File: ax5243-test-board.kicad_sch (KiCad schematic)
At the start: 39 parts, among them J1 Conn_Coaxial, J2 Conn_01x15, J3 Conn_01x15, U1 AX5243, X1 12MHz

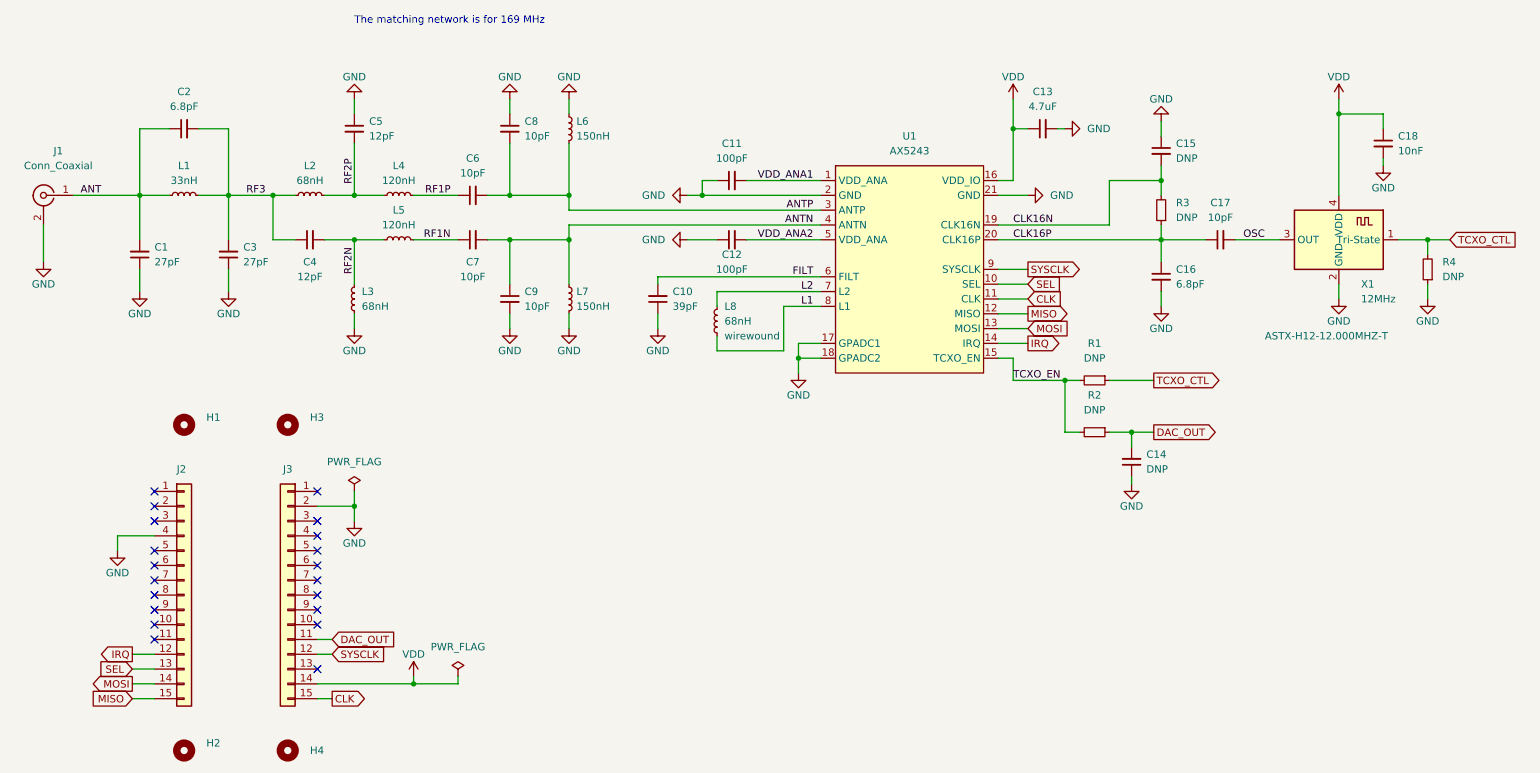
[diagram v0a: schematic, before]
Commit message: Add part numbers and Digikey SKUs
Also change TCXO frequency to 26 MHz.
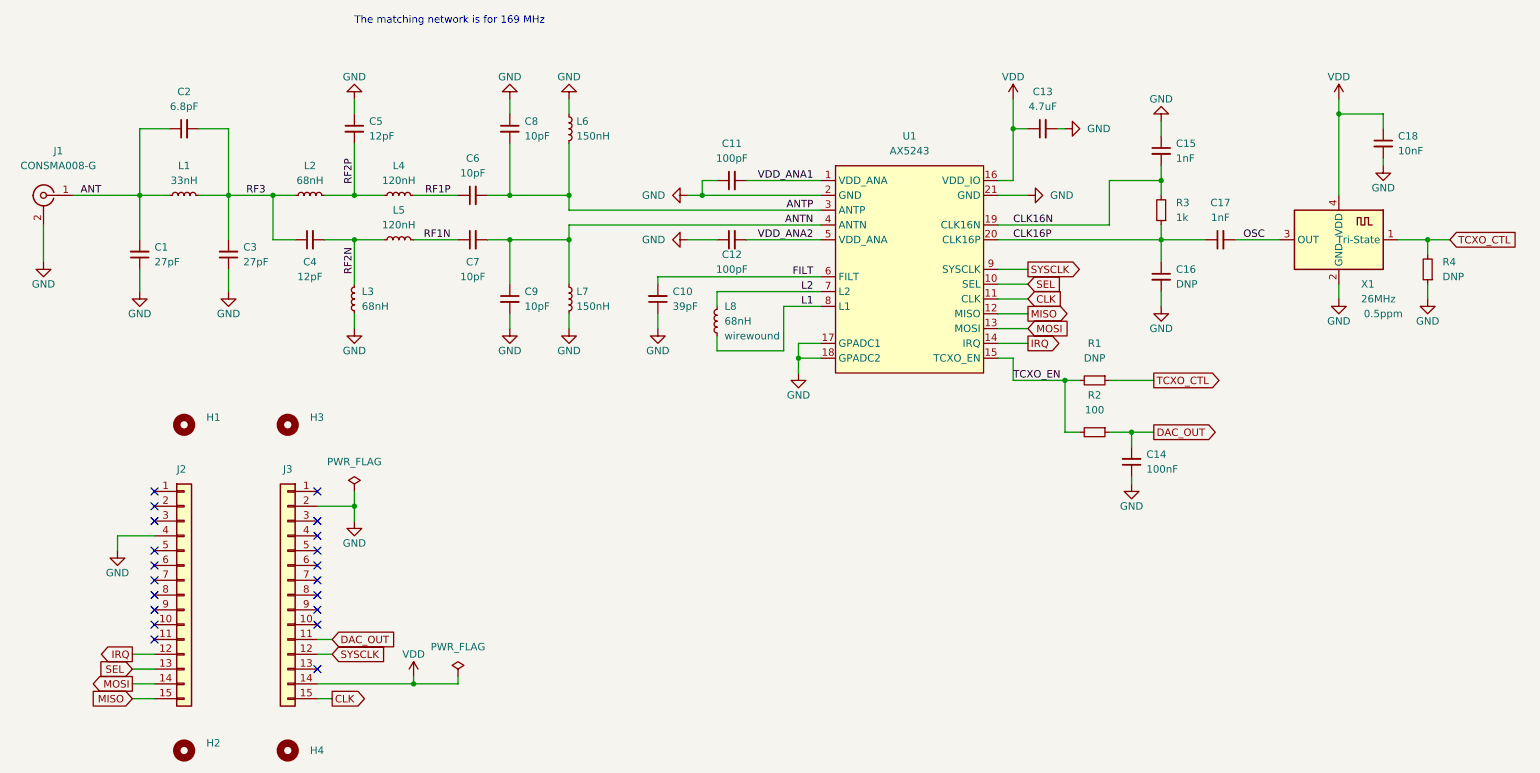
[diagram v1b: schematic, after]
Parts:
- C1, C3: MFT Name (none) -> Murata; MFT Number (none) -> GJM1555C1H270FB01D; SKU (none) -> 490-16380-1-ND; Vendor (none) -> Digikey
- C10: MFT Name (none) -> Murata; MFT Number (none) -> GJM1555C1H390JB01D; SKU (none) -> 490-17673-1-ND; Vendor (none) -> Digikey
- C11, C12: MFT Name (none) -> Murata; MFT Number (none) -> GCM1555C1H101GA16D; SKU (none) -> 490-GCM1555C1H101GA16DCT-ND; Vendor (none) -> Digikey
- C13: MFT Name (none) -> Murata; MFT Number (none) -> GRM188R61E475KE11D; SKU (none) -> 490-7203-1-ND; Vendor (none) -> Digikey
- C14: value DNP -> 100nF; MFT Name (none) -> Murata; MFT Number (none) -> GRM155R71H104KE14D; SKU (none) -> 490-10700-1-ND; Vendor (none) -> Digikey
- C15: value DNP -> 1nF; MFT Name (none) -> Murata; MFT Number (none) -> GRM1555C1H102GA01D; SKU (none) -> 490-8181-1-ND; Vendor (none) -> Digikey
- C16: value 6.8pF -> DNP; Config (none) -> DNP
- C17: value 10pF -> 1nF; MFT Name (none) -> Murata; MFT Number (none) -> GRM1555C1H102GA01D; SKU (none) -> 490-8181-1-ND; Vendor (none) -> Digikey
- C18: MFT Name (none) -> Murata; MFT Number (none) -> GRM155R71H103KA88J; SKU (none) -> 490-6351-1-ND; Vendor (none) -> Digikey
- C2: MFT Name (none) -> Murata; MFT Number (none) -> GJM1555C1H6R8CB01D; SKU (none) -> 490-3106-1-ND; Vendor (none) -> Digikey
- C4, C5: MFT Name (none) -> Murata; MFT Number (none) -> GJM1555C1H120JB01D; SKU (none) -> 490-3115-1-ND; Vendor (none) -> Digikey
- C6, C7, C8, C9: MFT Name (none) -> Murata; MFT Number (none) -> GJM1555C1H100FB01D; SKU (none) -> 490-11189-1-ND; Vendor (none) -> Digikey
- J1: value Conn_Coaxial -> CONSMA008-G; MFT Name (none) -> Linx Technologies; MFT Number (none) -> CONSMA008-G; SKU (none) -> CONSMA008-G-ND; Vendor (none) -> Digikey
- J2, J3: MFT Name (none) -> Harwin; MFT Number (none) -> M20-7821546; SKU (none) -> 952-2290-ND; Vendor (none) -> Digikey
- L1: MFT Name (none) -> Murata; MFT Number (none) -> LQW15AN33NH00D; SKU (none) -> 490-6805-1-ND; Vendor (none) -> Digikey
- L2, L3: MFT Name (none) -> Murata; MFT Number (none) -> LQW15AN68NG00D; SKU (none) -> 490-6837-1-ND; Vendor (none) -> Digikey
- L4, L5: MFT Name (none) -> Murata; MFT Number (none) -> LQW15ANR12J00D; SKU (none) -> 490-4091-1-ND; Vendor (none) -> Digikey
- L6, L7: MFT Name (none) -> Murata; MFT Number (none) -> LQW18ANR15J00D; SKU (none) -> 490-6924-1-ND; Vendor (none) -> Digikey
- L8: MFT Name (none) -> Murata; MFT Number (none) -> LQW18AN68NG00D; SKU (none) -> 490-6904-1-ND; Vendor (none) -> Digikey
- R1, R4: Config (none) -> DNP
- R2: value DNP -> 100; MFT Name (none) -> Yageo; MFT Number (none) -> RC0402FR-07100RP; SKU (none) -> YAG1248CT-ND; Vendor (none) -> Digikey
- R3: value DNP -> 1k; MFT Name (none) -> Yageo; MFT Number (none) -> RC0402FR-071KP; SKU (none) -> YAG1254CT-ND; Vendor (none) -> Digikey
- U1: MFT Name (none) -> ON Semiconductor; MFT Number (none) -> AX5243-1-TW30; SKU (none) -> 488-AX5243-1-TW30CT-ND; Vendor (none) -> Digikey
- X1: value 12MHz -> 26MHz; MFT Name Abracom -> Taitien; MFT Number ASTX-H12-12.000MHZ-T -> TYETACSANF-26.000000; Rating (none) -> 0.5ppm; SKU (none) -> 1664-1297-1-ND; Vendor (none) -> Digikey

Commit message: New kicad nigtly version
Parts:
- J1: MFT Number CONSMA008-G -> (none)
- X1: Rating 0.5ppm -> (none)

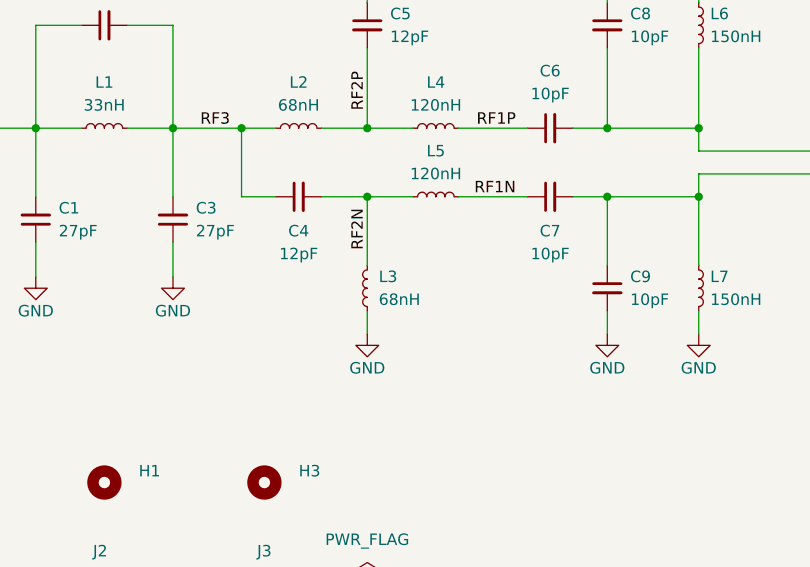
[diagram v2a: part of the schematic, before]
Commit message: Add additional matching capacitor needed for higher frequencies
This closes: #3
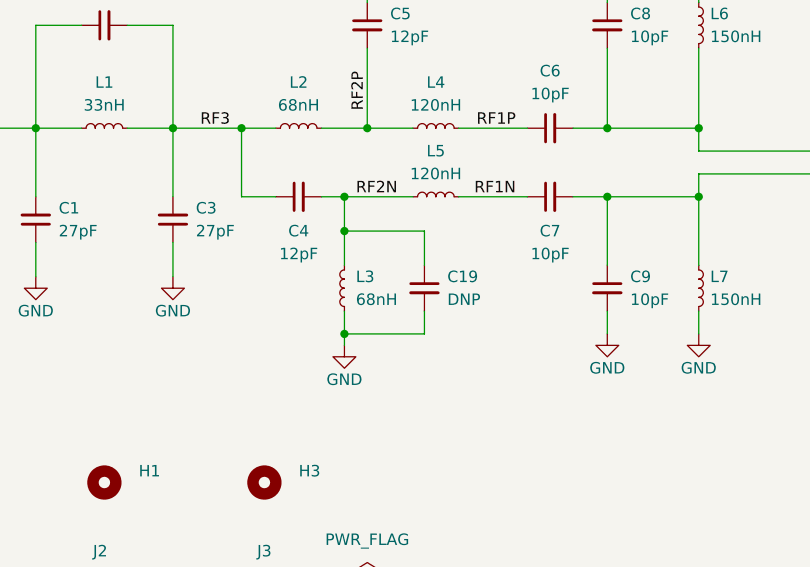
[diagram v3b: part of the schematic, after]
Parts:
- added C19: DNP, Capacitor_SMD:C_0402_1005Metric, symbol Device:C_Small
- C1, C10, C11, C12, C13, C14, C15, C17, C18, C2, C3, C4, C5, C6, C7, C8, C9, J2, J3, L1, L2, L3, L4, L5, L6, L7, R2, R3, U1: Vendor Digikey -> (none)
- L8: MFT Name Murata -> (none)
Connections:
- net GND: now also C19.2
- net RF2N: now also C19.1
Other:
- moved on the sheet: L3
